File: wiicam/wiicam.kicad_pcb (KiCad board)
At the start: 2 copper layers, 46.2 x 12.2 mm, 10 parts, among them J1 Conn_01x04_Male, U1 LF33_TO220, U2 wiimote_ir_camera, X1 ACO-xxxMHz

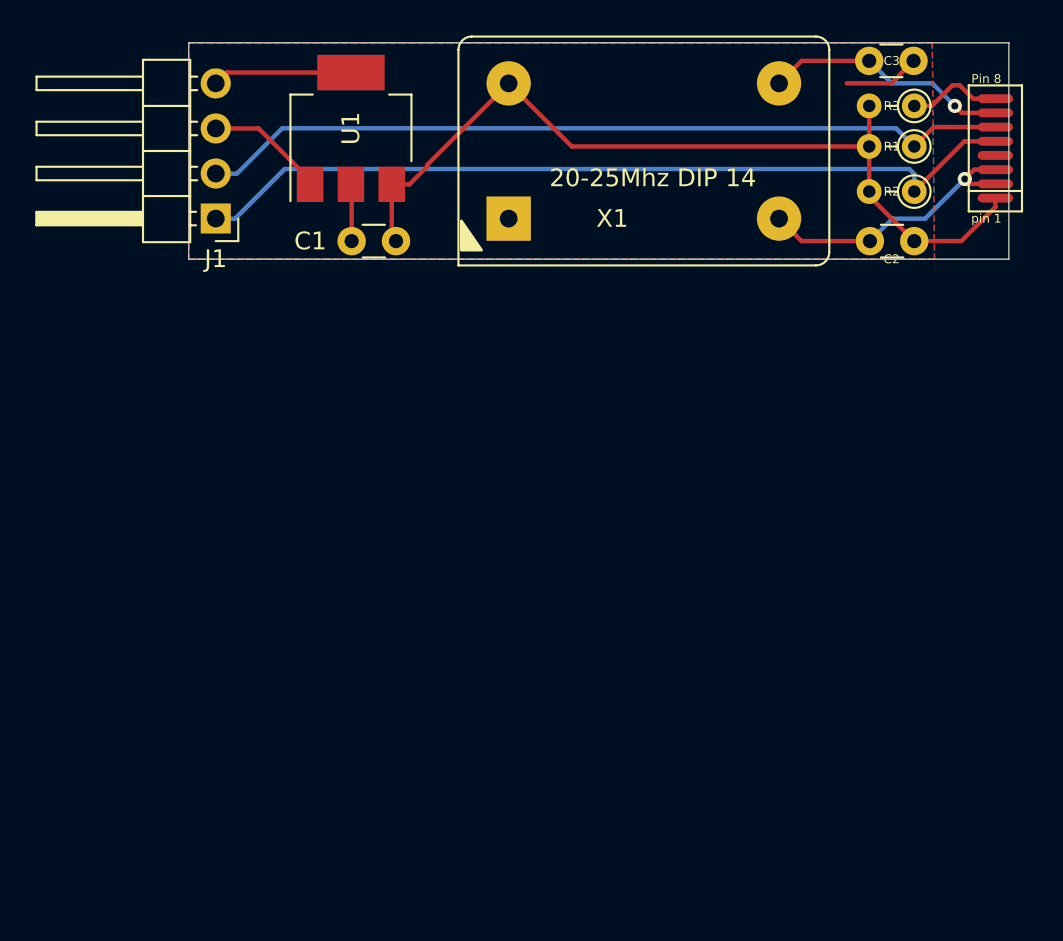
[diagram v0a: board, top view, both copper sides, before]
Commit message: Update PCB to SMD components and new footprint
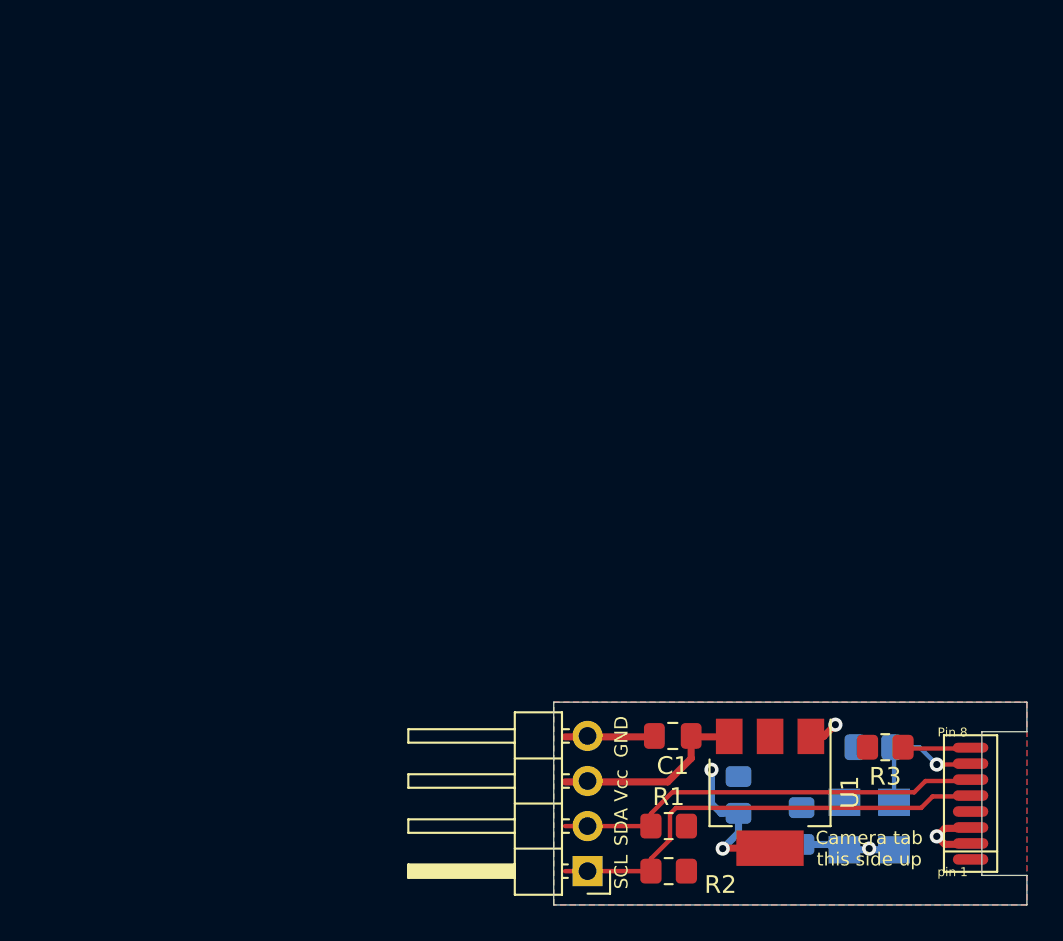
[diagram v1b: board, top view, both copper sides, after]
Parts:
- added C4: 10nF, Capacitor_SMD:C_0805_2012Metric_Pad1.18x1.45mm_HandSolder, B.Cu at (159.0, 121.2)
- C1: footprint Capacitor_THT:C_Disc_D3.0mm_W1.6mm_P2.50mm -> Capacitor_SMD:C_0805_2012Metric_Pad1.18x1.45mm_HandSolder
- C2: value 10nF -> 10uF; footprint Capacitor_THT:C_Disc_D3.0mm_W1.6mm_P2.50mm -> Capacitor_SMD:C_0805_2012Metric_Pad1.18x1.45mm_HandSolder; moved to B.Cu
- C3: footprint Capacitor_THT:C_Disc_D3.0mm_W1.6mm_P2.50mm -> Capacitor_SMD:C_0805_2012Metric_Pad1.18x1.45mm_HandSolder; moved to B.Cu
- R1, R2, R3: footprint Resistor_THT:R_Axial_DIN0204_L3.6mm_D1.6mm_P2.54mm_Vertical -> Resistor_SMD:R_0805_2012Metric_Pad1.20x1.40mm_HandSolder
- U1: value LF33_TO220 -> AMS1117-3.3; footprint Package_TO_SOT_SMD:SOT-223 -> Package_TO_SOT_SMD:SOT-223-3_TabPin2
- X1: value ACO-xxxMHz -> S53305-25.000-X; footprint Oscillator:Oscillator_DIP-14_LargePads -> Oscillator:Oscillator_SMD_TXC_7C-4Pin_5.0x3.2mm_HandSoldering; moved to B.Cu
- moved U1 44.2 mm to (153.2, 123.8), turned to 270 degrees
- moved C3 43.3 mm to (154.9, 125.7), turned to 90 degrees
- moved J1 42.3 mm to (142.9, 128.2)
- moved R1 40.7 mm to (147.4, 125.7), turned to 0 degrees
- moved R2 40.7 mm to (147.4, 128.2), turned to 0 degrees
- moved X1 39.8 mm to (158.8, 125.7), turned to 90 degrees
- moved U2 37.0 mm to (164.5, 124.4)
- moved R3 36.2 mm to (159.7, 121.2)
- moved C2 32.7 mm to (151.4, 123.9), turned to 90 degrees
- moved C1 32.0 mm to (147.7, 120.6)
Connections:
- C1 pad 1: 3v3 -> VCC
- C3 pad 1: CLK -> 3v3
- U1 pad 1: VCC -> GND
- U1 pad 2: GND -> 3v3
- U1 pad 3: 3v3 -> VCC
- U2 pad 4: Net-(U2-Pad4) -> (no net)
- X1 pad 1: Net-(X1-Pad1) -> 3v3
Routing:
- net 3v3: track 48.6 -> 14.1 mm, vias 0 -> 3
- net i2c_SDA: track 45.9 -> 24.3 mm
- net i2c_SCL: track 47.4 -> 25.9 mm
- net GND: track 32.4 -> 10.9 mm, vias 1 -> 2
- net CLK: track 13.9 -> 8.01 mm
- net VCC: track 6.77 -> 11.0 mm
- net Net-(R3-Pad1): track 6.11 -> 3.84 mm
- added copper zone on F.Cu, net 3v3
- removed copper zone on F.Cu, net GND
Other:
- board size 46.2 x 12.2 mm -> 26.7 x 11.4 mm
- board text added: "Camera tab this side up"
- board text added: "Wiimote IR camera board Original design by Mysli0210 of OKK-Design SMD update by PB"
- board text removed: "20-25Mhz DIP 14"
- board text removed: "Wiimote IR camera board Designed by Mysli0210 of OKK-Design"

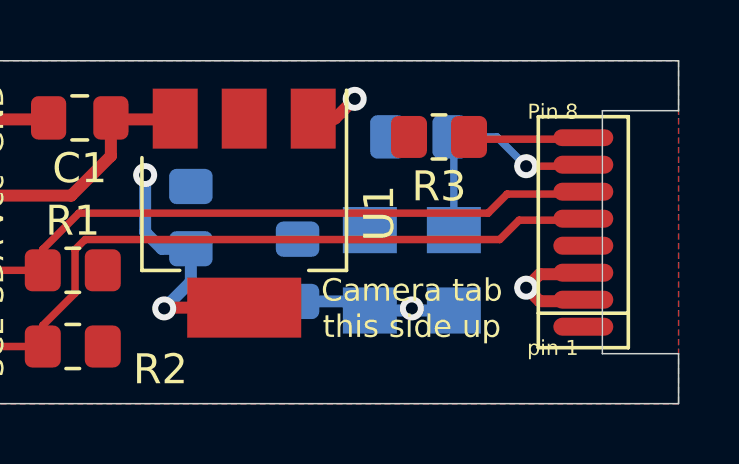
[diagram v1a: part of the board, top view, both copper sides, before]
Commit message: Remove OSC output capacitor Output capacitor value is too high - S53305-25.000-X is rated at max 15pF output load
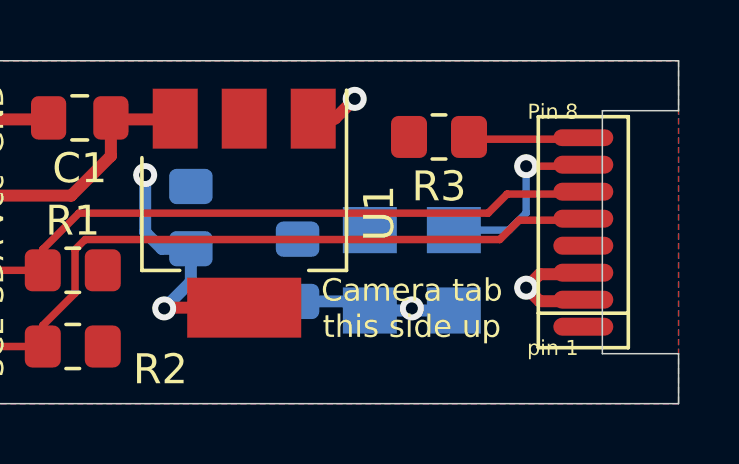
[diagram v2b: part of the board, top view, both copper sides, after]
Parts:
- removed C4: 10nF, Capacitor_SMD:C_0805_2012Metric_Pad1.18x1.45mm_HandSolder
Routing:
- net CLK: track 8.01 -> 6.11 mm
